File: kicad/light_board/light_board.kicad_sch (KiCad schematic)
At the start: 16 parts

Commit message: traffic lights WIP
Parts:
- removed J? (x3): Conn_01x01_Male, symbol Connector:Conn_01x01_Male
- added D2, D4: LED, symbol Device:LED
- added H1, H2, H3, H4: MountingHole, symbol Mechanical:MountingHole
- added J6: MCU_Bike, symbol Connector:Conn_01x01_Male
- added J7: 5V, symbol Connector:Conn_01x01_Male
- added Q2, Q4: FDD8453LZ, Package_TO_SOT_SMD:SOT-223-3_TabPin2, symbol Transistor_FET:BSP89
- added R2, R3: R_Small, symbol Device:R_Small
- J1: renamed from J?; value Conn_01x01_Male -> 24V
- J2: renamed from J?; value Conn_01x01_Male -> GND
- J3: renamed from J?; value Conn_01x01_Male -> MCU_L1
- J4: renamed from J?; value Conn_01x01_Male -> MCU_L2
- J5: renamed from J?; value Conn_01x01_Male -> MCU_L3
- K1: renamed from K?; value ADW11 -> J104D
- Q1: renamed from Q?; value BSP89 -> FDD8453LZ
- gave numbers to parts that had none: 6
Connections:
- net mcu is gone; now on net L1: Q1.1 (G)
- net +24V: now also J1.1 (Pin_1), Q2.2 (D), Q4.2 (D)
- net +5V: now also J7.1 (Pin_1)
- net GND: now also J2.1 (Pin_1), D2.1 (K), D4.1 (K)
- net L1: now reaches J3.1 (Pin_1)
- net L2: now reaches J4.1 (Pin_1)
- net L2: now also Q2.1 (G)
- net L3: now reaches J5.1 (Pin_1)
- net L3: now also Q4.1 (G)
- net mcu1 renamed Bike
- net Bike: now also J6.1 (Pin_1)
- new net: Q2.3 (S), R2.1
- new net: D4.2 (A), R3.2
- new net: Q4.3 (S), R3.1
- new net: D2.2 (A), R2.2
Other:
- note added: "Bike Light"
- note added: "Mounting Holes"
- note added: "Traffic Lights"
- note added: "spade connectors for lights"
- moved on the sheet: D1, D3, D5, J1, J2, J3, J4, J5, K1, Q1, Q3, R1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

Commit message: light board done
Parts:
- removed D1, D2, D4, D5: LED, symbol Device:LED
- removed R1, R2, R3, R4: R_Small, symbol Device:R_Small
- added J10, J11, J8, J9: Screw_Terminal_01x02, TerminalBlock:TerminalBlock_Altech_AK300-2_P5.00mm, symbol Connector:Screw_Terminal_01x02
- added J12: VAC, Connector_PinHeader_2.54mm:PinHeader_1x01_P2.54mm_Vertical, symbol Connector:Conn_01x01_Male
- added J13: NEUTRAL, Connector_PinHeader_2.54mm:PinHeader_1x01_P2.54mm_Vertical, symbol Connector:Conn_01x01_Male
- D3: value D -> SBR1A20T5-7; footprint (none) -> Diode_SMD:D_SOD-523
- H1, H2, H3, H4: footprint (none) -> MountingHole:MountingHole_3.5mm
- J1, J2, J3, J4, J5, J6, J7: footprint (none) -> Connector_PinHeader_2.54mm:PinHeader_1x01_P2.54mm_Vertical
- K1: value J104D -> 1462041-7; footprint Relay_THT:Relay_1P1T_NO_10x24x18.8mm_Panasonic_ADW11xxxxW_THT -> _mine:1462041-7
- Q1, Q2, Q3, Q4: footprint Package_TO_SOT_SMD:SOT-223-3_TabPin2 -> Package_TO_SOT_SMD:TO-252-2
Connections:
- net GND: now also J10.2 (Pin_2), J8.2 (Pin_2), J9.2 (Pin_2)
- net VAC: now also J12.1 (Pin_1)
- net at Q2.3 (S): now also J9.1 (Pin_1)
- net at Q4.3 (S): now also J10.1 (Pin_1)
- net at Q1.3 (S): now also J8.1 (Pin_1)
- net at K1.5: now also J11.1 (Pin_1)
- new net GND1: J11.2 (Pin_2), J13.1 (Pin_1)
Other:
- note added: "Connectors"
- note removed: "spade connectors for lights"
- moved on the sheet: D3, J1, J2, J3, J4, J5, J6, J7, K1, Q3

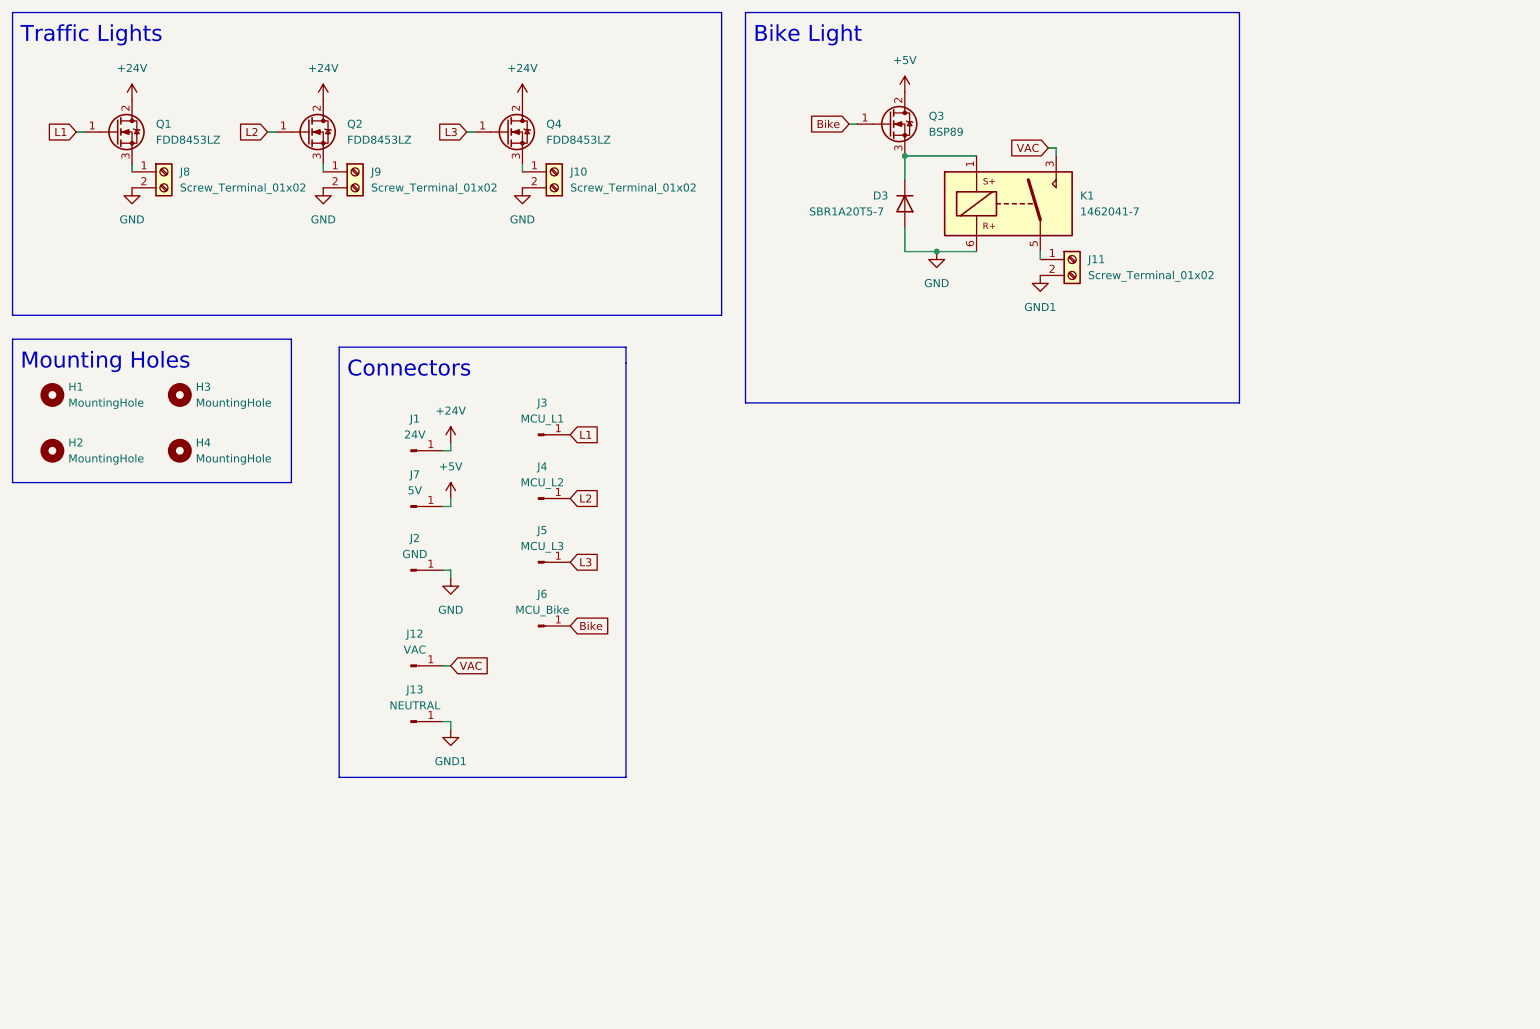
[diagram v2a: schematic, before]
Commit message: added isolation to power and light boards
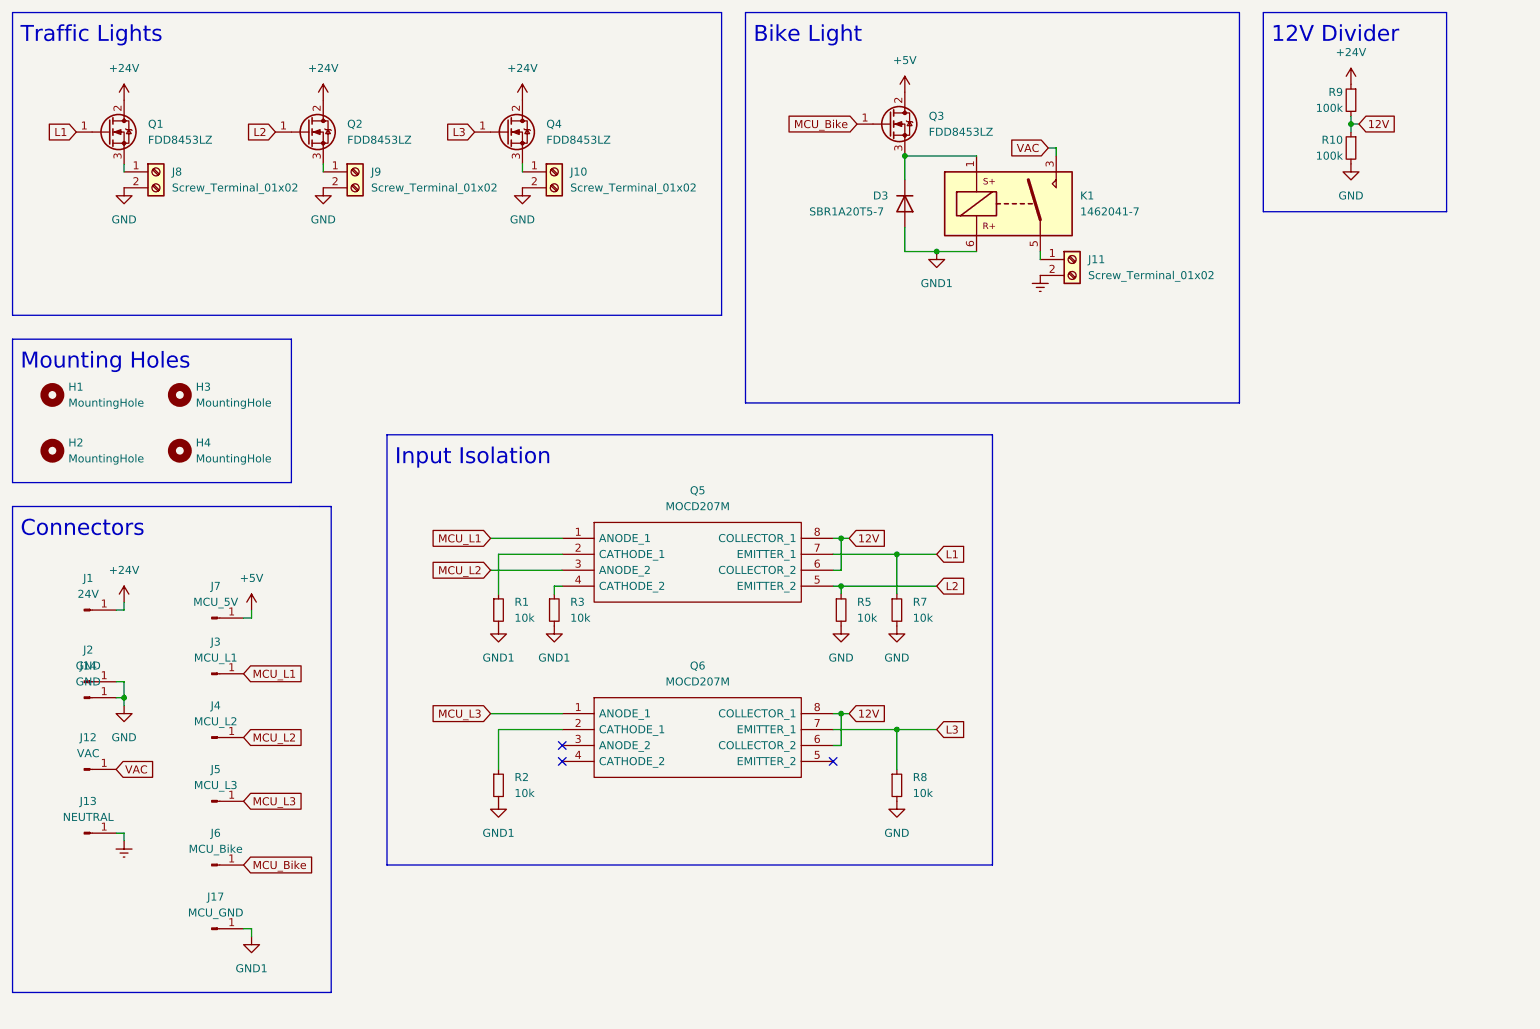
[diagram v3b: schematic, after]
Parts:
- added J14: GND, Connector_PinHeader_2.54mm:PinHeader_1x01_P2.54mm_Vertical, symbol Connector:Conn_01x01_Male
- added J17: MCU_GND, Connector_PinHeader_2.54mm:PinHeader_1x01_P2.54mm_Vertical, symbol Connector:Conn_01x01_Male
- added Q5, Q6: MOCD207M, Package_SO:SOIC-8_3.9x4.9mm_P1.27mm, symbol _mine:MOCD207M
- added R1, R2, R3, R5, R7, R8: 10k, Resistor_SMD:R_0805_2012Metric, symbol Device:R_Small
- added R10, R9: 100k, Resistor_SMD:R_1206_3216Metric, symbol Device:R_Small
- J7: value 5V -> MCU_5V
- Q3: value BSP89 -> FDD8453LZ
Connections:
- net +24V: now also R9.1
- net GND: now also J14.1 (Pin_1), R10.2, R5.2, R7.2, R8.2; no longer D3.2 (A), K1.6
- net GND1: now also D3.2 (A), K1.6, J17.1 (Pin_1), R1.2, R2.2, R3.2; no longer J11.2 (Pin_2), J13.1 (Pin_1)
- net L1: now also Q5.7 (EMITTER_1), R7.1; no longer J3.1 (Pin_1)
- net L2: now also Q5.5 (EMITTER_2), R5.1; no longer J4.1 (Pin_1)
- net L3: now also Q6.7 (EMITTER_1), R8.1; no longer J5.1 (Pin_1)
- net Bike renamed MCU_Bike
- new net: Q5.4 (CATHODE_2), R3.1
- new net: Q5.2 (CATHODE_1), R1.1
- new net: Q6.2 (CATHODE_1), R2.1
- new net 12V: Q5.6 (COLLECTOR_2), Q5.8 (COLLECTOR_1), Q6.6 (COLLECTOR_2), Q6.8 (COLLECTOR_1), R10.1, R9.2
- new net Earth: J11.2 (Pin_2), J13.1 (Pin_1)
- new net MCU_L1: J3.1 (Pin_1), Q5.1 (ANODE_1)
- new net MCU_L2: J4.1 (Pin_1), Q5.3 (ANODE_2)
- new net MCU_L3: J5.1 (Pin_1), Q6.1 (ANODE_1)
- no-connect marks 0 -> 3
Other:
- note added: "12V Divider"
- note added: "Input Isolation"
- moved on the sheet: J1, J12, J13, J2, J3, J4, J5, J6, J7, J8, Q1

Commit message: light board v2 wip, 3/25/22
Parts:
- removed Q3: FDD8453LZ, Package_TO_SOT_SMD:TO-252-2, symbol Transistor_FET:BSP89
- R1, R2, R3: value 10k -> 150
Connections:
- net +24V: now also J10.1 (Pin_1), J8.1 (Pin_1), J9.1 (Pin_1); no longer Q1.2 (D), Q2.2 (D), Q4.2 (D)
- net Earth: now also K1.3; no longer J11.2 (Pin_2)
- net GND: now also Q1.3 (S), Q2.3 (S), Q4.3 (S); no longer J10.2 (Pin_2), J8.2 (Pin_2), J9.2 (Pin_2)
- net GND1: now also K1.1; no longer K1.6
- net MCU_Bike: now also D3.1 (K), K1.6
- net VAC: now also J11.1 (Pin_1); no longer K1.3
- net at K1.5: now also J11.2 (Pin_2); no longer J11.1 (Pin_1)
- new net: J9.2 (Pin_2), Q2.2 (D)
- new net: J10.2 (Pin_2), Q4.2 (D)
- new net: J8.2 (Pin_2), Q1.2 (D)
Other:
- moved on the sheet: J10, J11, J8, J9, Q1, Q2, Q4

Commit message: light board v2
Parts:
- removed J7: MCU_5V, Connector_PinHeader_2.54mm:PinHeader_1x01_P2.54mm_Vertical, symbol Connector:Conn_01x01_Male
- removed R10, R9: 100k, Resistor_SMD:R_1206_3216Metric, symbol Device:R_Small
- added J15: 5V, Connector_PinHeader_2.54mm:PinHeader_1x01_P2.54mm_Vertical, symbol Connector:Conn_01x01_Male
- added J16: GND, Connector_PinHeader_2.54mm:PinHeader_1x01_P2.54mm_Vertical, symbol Connector:Conn_01x01_Male
- added JP1, JP2, JP3, JP4: SolderJumper_2_Open, Jumper:SolderJumper-2_P1.3mm_Open_TrianglePad1.0x1.5mm, symbol Jumper:SolderJumper_2_Open
- D3: value SBR1A20T5-7 -> MBR130HW; footprint Diode_SMD:D_SOD-523 -> Diode_SMD:D_SOD-123
- R1, R2, R3: footprint Resistor_SMD:R_0805_2012Metric -> Resistor_SMD:R_0603_1608Metric
- R5, R7, R8: value 10k -> 1k; footprint Resistor_SMD:R_0805_2012Metric -> Resistor_SMD:R_0603_1608Metric
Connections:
- net 12V is gone; now on net +5V: Q5.6 (COLLECTOR_2), Q5.8 (COLLECTOR_1), Q6.6 (COLLECTOR_2), Q6.8 (COLLECTOR_1)
- net +5V: now also J15.1 (Pin_1)
- net GND: now also J16.1 (Pin_1), JP4.2 (B)
- net GND1: now also JP4.1 (A)
- net L1: now also JP1.2 (B)
- net L2: now also JP2.2 (B)
- net L3: now also JP3.2 (B)
- net MCU_L1: now also JP1.1 (A)
- net MCU_L2: now also JP2.1 (A)
- net MCU_L3: now also JP3.1 (A)
- net VAC: now also J11.2 (Pin_2); no longer J11.1 (Pin_1)
- net at K1.5: now also J11.1 (Pin_1); no longer J11.2 (Pin_2)
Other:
- note added: "Note: If using, do not populate input isolation components"
- note added: "Optional Jumpers"
- note removed: "12V Divider"
- moved on the sheet: Q5, Q6, R1, R2, R3, R5, R7, R8

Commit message: update pcbs
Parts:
- removed J14: GND, Connector_PinHeader_2.54mm:PinHeader_1x01_P2.54mm_Vertical, symbol Connector:Conn_01x01_Male
- J1, J12, J13, J2: footprint Connector_PinHeader_2.54mm:PinHeader_1x01_P2.54mm_Vertical -> _mylib:hole
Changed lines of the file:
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@@
   (junction (at 166.37 55.88) (diameter 0) (color 0 0 0 0)
-  )
-  (junction (at 36.83 127) (diameter 0) (color 0 0 0 0)
   )
   (junction (at 146.05 93.98) (diameter 0) (color 0 0 0 0)
@@
   (no_connect (at 144.78 121.92))
   (no_connect (at 101.6 119.38))
-  (wire (pts (xy 36.83 127) (xy 36.83 128.27))
-    (stroke (width 0) (type default) (color 0 0 0 0))
-  )
   (wire (pts (xy 146.05 86.36) (xy 144.78 86.36))
     (stroke (width 0) (type default) (color 0 0 0 0))
@@
     (stroke (width 0) (type default) (color 0 0 0 0))
   )
-  (wire (pts (xy 35.56 127) (xy 36.83 127))
-    (stroke (width 0) (type default) (color 0 0 0 0))
-  )
   (wire (pts (xy 146.05 93.98) (xy 146.05 95.25))
     (stroke (width 0) (type default) (color 0 0 0 0))
@@
     (stroke (width 0) (type default) (color 0 0 0 0))
   )
-  (wire (pts (xy 36.83 124.46) (xy 36.83 127))
+  (wire (pts (xy 36.83 124.46) (xy 36.83 125.73))
     (stroke (width 0) (type default) (color 0 0 0 0))
   )
@@
     (property "Reference" "J12" (id 0) (at 31.115 133.35 0))
     (property "Value" "VAC" (id 1) (at 31.115 135.89 0))
-    (property "Footprint" "Connector_PinHeader_2.54mm:PinHeader_1x01_P2.54mm_Vertical" (id 2) (at 30.48 138.43 0)
+    (property "Footprint" "_mylib:hole" (id 2) (at 30.48 138.43 0)
       (effects (font (size 1.27 1.27)) hide)
     )
@@
     (property "Reference" "J2" (id 0) (at 31.115 119.38 0))
     (property "Value" "GND" (id 1) (at 31.115 121.92 0))
-    (property "Footprint" "Connector_PinHeader_2.54mm:PinHeader_1x01_P2.54mm_Vertical" (id 2) (at 30.48 124.46 0)
+    (property "Footprint" "_mylib:hole" (id 2) (at 30.48 124.46 0)
       (effects (font (size 1.27 1.27)) hide)
     )
@@
     (property "Reference" "J1" (id 0) (at 31.115 107.95 0))
     (property "Value" "24V" (id 1) (at 31.115 110.49 0))
-    (property "Footprint" "Connector_PinHeader_2.54mm:PinHeader_1x01_P2.54mm_Vertical" (id 2) (at 30.48 113.03 0)
+    (property "Footprint" "_mylib:hole" (id 2) (at 30.48 113.03 0)
       (effects (font (size 1.27 1.27)) hide)
     )
@@
     (pin "1")
   )
-  (symbol (lib_id "power:GND") (at 36.83 128.27 0) (unit 1)
-    (in_bom yes) (on_board yes) (fields_autoplaced)
-    (property "Reference" "#PWR013" (id 0) (at 36.83 134.62 0)
-      (effects (font (size 1.27 1.27)) hide)
-    )
-    (property "Value" "GND" (id 1) (at 36.83 133.35 0))
-    (property "Footprint" "" (id 2) (at 36.83 128.27 0)
-      (effects (font (size 1.27 1.27)) hide)
-    )
-    (property "Datasheet" "" (id 3) (at 36.83 128.27 0)
+  (symbol (lib_id "power:GND") (at 36.83 125.73 0) (unit 1)
+    (in_bom yes) (on_board yes) (fields_autoplaced)
+    (property "Reference" "#PWR013" (id 0) (at 36.83 132.08 0)
+      (effects (font (size 1.27 1.27)) hide)
+    )
+    (property "Value" "GND" (id 1) (at 36.83 130.81 0))
+    (property "Footprint" "" (id 2) (at 36.83 125.73 0)
+      (effects (font (size 1.27 1.27)) hide)
+    )
+    (property "Datasheet" "" (id 3) (at 36.83 125.73 0)
       (effects (font (size 1.27 1.27)) hide)
     )
@@
     (property "Reference" "J13" (id 0) (at 31.115 143.51 0))
     (property "Value" "NEUTRAL" (id 1) (at 31.115 146.05 0))
-    (property "Footprint" "Connector_PinHeader_2.54mm:PinHeader_1x01_P2.54mm_Vertical" (id 2) (at 30.48 148.59 0)
+    (property "Footprint" "_mylib:hole" (id 2) (at 30.48 148.59 0)
       (effects (font (size 1.27 1.27)) hide)
     )
@@
     (pin "1")
     (pin "2")
-  )
-  (symbol (lib_id "Connector:Conn_01x01_Male") (at 30.48 127 0) (unit 1)
-    (in_bom yes) (on_board yes) (fields_autoplaced)
-    (property "Reference" "J14" (id 0) (at 31.115 121.92 0))
-    (property "Value" "GND" (id 1) (at 31.115 124.46 0))
-    (property "Footprint" "Connector_PinHeader_2.54mm:PinHeader_1x01_P2.54mm_Vertical" (id 2) (at 30.48 127 0)
-      (effects (font (size 1.27 1.27)) hide)
-    )
-    (property "Datasheet" "~" (id 3) (at 30.48 127 0)
-      (effects (font (size 1.27 1.27)) hide)
-    )
-    (pin "1")
   )
   (symbol (lib_id "_mine:MOCD207M") (at 101.6 86.36 0) (unit 1)
@@
     )
     (path "/3f03fd16-a09a-47f5-adca-50c300f3a91b"
-      (reference "J1") (unit 1) (value "24V") (footprint "Connector_PinHeader_2.54mm:PinHeader_1x01_P2.54mm_Vertical")
+      (reference "J1") (unit 1) (value "24V") (footprint "_mylib:hole")
     )
     (path "/2ebe7d52-7c41-4411-b9ef-dfc7a0409ee4"
-      (reference "J2") (unit 1) (value "GND") (footprint "Connector_PinHeader_2.54mm:PinHeader_1x01_P2.54mm_Vertical")
+      (reference "J2") (unit 1) (value "GND") (footprint "_mylib:hole")
     )
     (path "/6bc02308-6fbd-49c8-811d-539d13503d44"
@@
     )
     (path "/264d4db4-f564-46bd-9b21-cfd66b695585"
-      (reference "J12") (unit 1) (value "VAC") (footprint "Connector_PinHeader_2.54mm:PinHeader_1x01_P2.54mm_Vertical")
+      (reference "J12") (unit 1) (value "VAC") (footprint "_mylib:hole")
     )
     (path "/5378bcb6-accb-4c3e-aaff-ae0cd065931f"
-      (reference "J13") (unit 1) (value "NEUTRAL") (footprint "Connector_PinHeader_2.54mm:PinHeader_1x01_P2.54mm_Vertical")
-    )
-    (path "/c99e6d80-f2a9-415e-92b3-df98c4f485fa"
-      (reference "J14") (unit 1) (value "GND") (footprint "Connector_PinHeader_2.54mm:PinHeader_1x01_P2.54mm_Vertical")
+      (reference "J13") (unit 1) (value "NEUTRAL") (footprint "_mylib:hole")
     )
     (path "/385e0403-8b28-4505-873a-a91713d8181b"
